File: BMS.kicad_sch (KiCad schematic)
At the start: 36 parts, among them J2 BMS1OTP, J3 BMS2OTP, U1 EL3H7, U3 ISO1640BDR, U4 BQ7695201PFBR, U6 ISO1640BDR

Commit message: time flies when you're kicadding :(
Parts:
- C18, C19, C2, C20, C26: footprint Capacitor_SMD:C_0805_2012Metric_Pad1.18x1.45mm_HandSolder -> Capacitor_SMD:C_0805_2012Metric
- R13: footprint Resistor_SMD:R_0805_2012Metric -> Resistor_SMD:R_0805_2012Metric_Pad1.20x1.40mm_HandSolder
- R18, R19, R20: footprint Resistor_SMD:R_0805_2012Metric_Pad1.20x1.40mm_HandSolder -> Resistor_SMD:R_0805_2012Metric
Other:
- note added: "I2C Pullup resistors need to be on the OTP circuit"
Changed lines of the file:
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@@
     (effects (font (size 2.5 2.5) (thickness 0.5) bold) (justify left bottom))
+  )
+  (text "I2C Pullup resistors need to be \non the OTP circuit"
+    (at 104.14 87.63 0)
+    (effects (font (size 1.27 1.27)) (justify left bottom))
   )
   (label "cell16" (at 200.66 210.185 0) (fields_autoplaced)
@@
       (effects (font (size 1.27 1.27)) (justify right))
     )
-    (property "Footprint" "Capacitor_SMD:C_0805_2012Metric_Pad1.18x1.45mm_HandSolder" (at 284.1498 89.535 0)
+    (property "Footprint" "Capacitor_SMD:C_0805_2012Metric" (at 284.1498 89.535 0)
       (effects (font (size 1.27 1.27)) hide)
     )
@@
       (effects (font (size 1.27 1.27)) (justify right))
     )
-    (property "Footprint" "Capacitor_SMD:C_0805_2012Metric_Pad1.18x1.45mm_HandSolder" (at 372.4148 28.575 0)
+    (property "Footprint" "Capacitor_SMD:C_0805_2012Metric" (at 372.4148 28.575 0)
       (effects (font (size 1.27 1.27)) hide)
     )
@@
       (effects (font (size 1.27 1.27)) (justify right))
     )
-    (property "Footprint" "Capacitor_SMD:C_0805_2012Metric_Pad1.18x1.45mm_HandSolder" (at 111.4298 33.655 0)
+    (property "Footprint" "Capacitor_SMD:C_0805_2012Metric" (at 111.4298 33.655 0)
       (effects (font (size 1.27 1.27)) hide)
     )
@@
       (effects (font (size 1.27 1.27)))
     )
-    (property "Footprint" "Resistor_SMD:R_0805_2012Metric_Pad1.20x1.40mm_HandSolder" (at 384.429 27.559 90)
+    (property "Footprint" "Resistor_SMD:R_0805_2012Metric" (at 384.429 27.559 90)
       (effects (font (size 1.27 1.27)) hide)
     )
@@
       (effects (font (size 1.27 1.27)) (justify right))
     )
-    (property "Footprint" "Capacitor_SMD:C_0805_2012Metric_Pad1.18x1.45mm_HandSolder" (at 30.7848 94.615 0)
+    (property "Footprint" "Capacitor_SMD:C_0805_2012Metric" (at 30.7848 94.615 0)
       (effects (font (size 1.27 1.27)) hide)
     )
@@
       (effects (font (size 1.27 1.27)))
     )
-    (property "Footprint" "Resistor_SMD:R_0805_2012Metric_Pad1.20x1.40mm_HandSolder" (at 342.011 44.831 90)
+    (property "Footprint" "Resistor_SMD:R_0805_2012Metric" (at 342.011 44.831 90)
       (effects (font (size 1.27 1.27)) hide)
     )
@@
       (effects (font (size 1.27 1.27)) (justify right))
     )
-    (property "Footprint" "Capacitor_SMD:C_0805_2012Metric_Pad1.18x1.45mm_HandSolder" (at 29.5148 133.35 0)
+    (property "Footprint" "Capacitor_SMD:C_0805_2012Metric" (at 29.5148 133.35 0)
       (effects (font (size 1.27 1.27)) hide)
     )
@@
       (effects (font (size 1.27 1.27)) (justify right))
     )
-    (property "Footprint" "Capacitor_SMD:C_0805_2012Metric_Pad1.18x1.45mm_HandSolder" (at 355.6 30.1498 0)
+    (property "Footprint" "Capacitor_SMD:C_0805_2012Metric" (at 355.6 30.1498 0)
       (effects (font (size 1.27 1.27)) hide)
     )
@@
       (effects (font (size 1.27 1.27)) (justify right))
     )
-    (property "Footprint" "Capacitor_SMD:C_0805_2012Metric_Pad1.18x1.45mm_HandSolder" (at 119.0752 140.97 0)
+    (property "Footprint" "Capacitor_SMD:C_0805_2012Metric" (at 119.0752 140.97 0)
       (effects (font (size 1.27 1.27)) hide)
     )
@@
       (effects (font (size 1.27 1.27)))
     )
-    (property "Footprint" "Resistor_SMD:R_0805_2012Metric_Pad1.20x1.40mm_HandSolder" (at 131.064 32.639 90)
+    (property "Footprint" "Resistor_SMD:R_0805_2012Metric" (at 131.064 32.639 90)
       (effects (font (size 1.27 1.27)) hide)
     )
@@
       (effects (font (size 1.27 1.27)) (justify right))
     )
-    (property "Footprint" "Capacitor_SMD:C_0805_2012Metric_Pad1.18x1.45mm_HandSolder" (at 389.5852 114.935 0)
+    (property "Footprint" "Capacitor_SMD:C_0805_2012Metric" (at 389.5852 114.935 0)
       (effects (font (size 1.27 1.27)) hide)
     )
@@
       (effects (font (size 1.27 1.27)))
     )
-    (property "Footprint" "Resistor_SMD:R_0805_2012Metric_Pad1.20x1.40mm_HandSolder" (at 88.646 49.911 90)
+    (property "Footprint" "Resistor_SMD:R_0805_2012Metric" (at 88.646 49.911 90)
       (effects (font (size 1.27 1.27)) hide)
     )
@@
       (effects (font (size 1.27 1.27)) (justify right))
     )
-    (property "Footprint" "Capacitor_SMD:C_0805_2012Metric_Pad1.18x1.45mm_HandSolder" (at 119.0498 33.655 0)
+    (property "Footprint" "Capacitor_SMD:C_0805_2012Metric" (at 119.0498 33.655 0)
       (effects (font (size 1.27 1.27)) hide)
     )
@@
       (effects (font (size 1.27 1.27)))
     )
-    (property "Footprint" "Resistor_SMD:R_0805_2012Metric_Pad1.20x1.40mm_HandSolder" (at 342.011 42.291 90)
+    (property "Footprint" "Resistor_SMD:R_0805_2012Metric" (at 342.011 42.291 90)
       (effects (font (size 1.27 1.27)) hide)
     )
@@
       (effects (font (size 1.27 1.27)) (justify right))
     )
-    (property "Footprint" "Resistor_SMD:R_0805_2012Metric" (at 358.14 151.765 0)
+    (property "Footprint" "Resistor_SMD:R_0805_2012Metric_Pad1.20x1.40mm_HandSolder" (at 358.14 151.765 0)
       (effects (font (size 1.27 1.27)) hide)
     )
@@
       (effects (font (size 1.27 1.27)) (justify right))
     )
-    (property "Footprint" "Capacitor_SMD:C_0805_2012Metric_Pad1.18x1.45mm_HandSolder" (at 364.7948 28.575 0)
+    (property "Footprint" "Capacitor_SMD:C_0805_2012Metric" (at 364.7948 28.575 0)
       (effects (font (size 1.27 1.27)) hide)
     )
@@
       (effects (font (size 1.27 1.27)) (justify right))
     )
-    (property "Footprint" "Capacitor_SMD:C_0805_2012Metric_Pad1.18x1.45mm_HandSolder" (at 102.235 35.2298 0)
+    (property "Footprint" "Capacitor_SMD:C_0805_2012Metric" (at 102.235 35.2298 0)
       (effects (font (size 1.27 1.27)) hide)
     )
@@
       (effects (font (size 1.27 1.27)))
     )
-    (property "Footprint" "Resistor_SMD:R_0805_2012Metric_Pad1.20x1.40mm_HandSolder" (at 88.646 47.371 90)
+    (property "Footprint" "Resistor_SMD:R_0805_2012Metric" (at 88.646 47.371 90)
       (effects (font (size 1.27 1.27)) hide)
     )
@@
       (effects (font (size 1.27 1.27)) (justify right))
     )
-    (property "Footprint" "Capacitor_SMD:C_0805_2012Metric_Pad1.18x1.45mm_HandSolder" (at 301.9298 107.95 0)
-      (effects (font (size 1.27 1.27)) hide)
-    )
+    (property "Footprint" "Capacitor_SMD:C_0805_2012Metric" (at 301.9298 107.95 0)
+      (effects (font (size 1.27 1.27)) hide)
+    )

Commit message: new ADC layout
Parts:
- renumbered C2 to C10, C26 to C11, C20 to C12, C19 to C13, C2 to C14, C2 to C3, C18 to C4, C26 to C5, C20 to C6, C2 to C7, C19 to C8, C18 to C9, R18 to R11, R19 to R12, R20 to R16, R18 to R5, R19 to R6, R20 to R9, U4 to U2, U4 to U5

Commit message: literal piss and shit
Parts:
- C10, C13, C14, C3, C7, C8: value 1u -> 1uF
- C11, C5: value .47u -> 0.47uF
- C12, C6: value 100p -> 100pF
- C4, C9: value 4.7u -> 4.7uF
- R13: footprint Resistor_SMD:R_0805_2012Metric_Pad1.20x1.40mm_HandSolder -> Resistor_SMD:R_0805_2012Metric
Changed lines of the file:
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@@
       (effects (font (size 1.27 1.27)) (justify right))
     )
-    (property "Value" "4.7u" (at 288.925 94.615 0)
+    (property "Value" "4.7uF" (at 288.925 94.615 0)
       (effects (font (size 1.27 1.27)) (justify right))
     )
@@
       (effects (font (size 1.27 1.27)) (justify right))
     )
-    (property "Value" "1u" (at 377.19 33.655 0)
+    (property "Value" "1uF" (at 377.19 33.655 0)
       (effects (font (size 1.27 1.27)) (justify right))
     )
@@
       (effects (font (size 1.27 1.27)) (justify right))
     )
-    (property "Value" "100p" (at 104.775 38.735 0)
+    (property "Value" "100pF" (at 104.775 38.735 0)
       (effects (font (size 1.27 1.27)) (justify right))
     )
@@
       (effects (font (size 1.27 1.27)) (justify right))
     )
-    (property "Value" "4.7u" (at 35.56 99.695 0)
+    (property "Value" "4.7uF" (at 35.56 99.695 0)
       (effects (font (size 1.27 1.27)) (justify right))
     )
@@
       (effects (font (size 1.27 1.27)) (justify right))
     )
-    (property "Value" "1u" (at 25.4 138.43 0)
+    (property "Value" "1uF" (at 25.4 138.43 0)
       (effects (font (size 1.27 1.27)) (justify right))
     )
@@
       (effects (font (size 1.27 1.27)) (justify right))
     )
-    (property "Value" ".47u" (at 349.25 34.925 90)
+    (property "Value" "0.47uF" (at 349.25 34.925 90)
       (effects (font (size 1.27 1.27)) (justify right))
     )
@@
       (effects (font (size 1.27 1.27)) (justify right))
     )
-    (property "Value" "1u" (at 125.095 135.89 0)
+    (property "Value" "1uF" (at 125.095 135.89 0)
       (effects (font (size 1.27 1.27)) (justify right))
     )
@@
       (effects (font (size 1.27 1.27)) (justify right))
     )
-    (property "Value" "1u" (at 394.97 109.855 0)
+    (property "Value" "1uF" (at 394.97 109.855 0)
       (effects (font (size 1.27 1.27)) (justify right))
     )
@@
       (effects (font (size 1.27 1.27)) (justify right))
     )
-    (property "Value" "1u" (at 123.825 38.735 0)
+    (property "Value" "1uF" (at 123.825 38.735 0)
       (effects (font (size 1.27 1.27)) (justify right))
     )
@@
       (effects (font (size 1.27 1.27)) (justify right))
     )
-    (property "Footprint" "Resistor_SMD:R_0805_2012Metric_Pad1.20x1.40mm_HandSolder" (at 358.14 151.765 0)
+    (property "Footprint" "Resistor_SMD:R_0805_2012Metric" (at 358.14 151.765 0)
       (effects (font (size 1.27 1.27)) hide)
     )
@@
       (effects (font (size 1.27 1.27)) (justify right))
     )
-    (property "Value" "100p" (at 358.14 33.655 0)
+    (property "Value" "100pF" (at 358.14 33.655 0)
       (effects (font (size 1.27 1.27)) (justify right))
     )
@@
       (effects (font (size 1.27 1.27)) (justify right))
     )
-    (property "Value" ".47u" (at 95.885 40.005 90)
+    (property "Value" "0.47uF" (at 95.885 40.005 90)
       (effects (font (size 1.27 1.27)) (justify right))
     )
@@
       (effects (font (size 1.27 1.27)) (justify right))
     )
-    (property "Value" "1u" (at 296.545 113.03 0)
-      (effects (font (size 1.27 1.27)) (justify right))
-    )
+    (property "Value" "1uF" (at 296.545 113.03 0)
+      (effects (font (size 1.27 1.27)) (justify right))
+    )

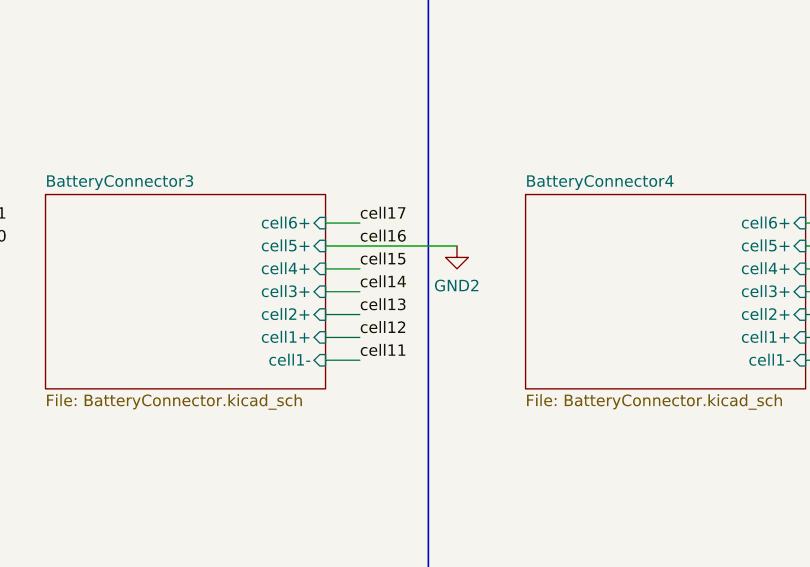
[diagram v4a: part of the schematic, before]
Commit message: fix gnd2
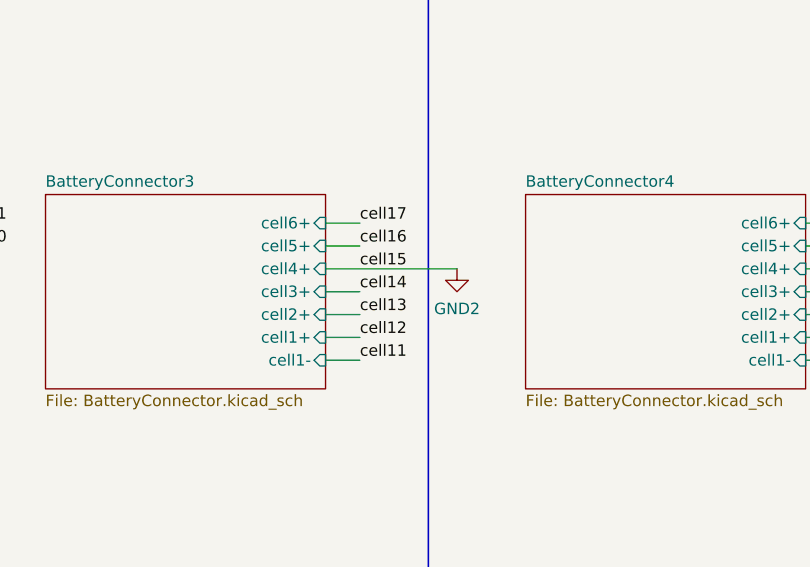
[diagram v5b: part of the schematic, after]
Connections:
- net cell15 is gone; now on net GND2: U2.1 (VC15)
- net GND2: no longer U2.48 (VC16), U5.16 (VC0)
- new net cell16: U2.48 (VC16), U5.16 (VC0)
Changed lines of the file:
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@@
-    (stroke (width 0) (type default))
-  )
-  (wire (pts (xy 196.85 210.185) (xy 211.455 210.185))
     (stroke (width 0) (type default))
   )
@@
     (stroke (width 0) (type default))
   )
+  (wire (pts (xy 196.85 210.185) (xy 200.66 210.185))
+    (stroke (width 0) (type default))
+  )
   (wire (pts (xy 294.64 212.725) (xy 298.45 212.725))
     (stroke (width 0) (type default))
@@
     (stroke (width 0) (type default))
   )
-  (wire (pts (xy 196.85 212.725) (xy 200.66 212.725))
+  (wire (pts (xy 196.85 212.725) (xy 211.455 212.725))
     (stroke (width 0) (type default))
   )
@@
     )
   )
-  (symbol (lib_id "power:GND2") (at 211.455 210.185 0) (unit 1)
+  (symbol (lib_id "power:GND2") (at 211.455 212.725 0) (unit 1)
     (in_bom yes) (on_board yes) (dnp no) (fields_autoplaced)
-    (property "Reference" "#PWR028" (at 211.455 216.535 0)
+    (property "Reference" "#PWR028" (at 211.455 219.075 0)
       (effects (font (size 1.27 1.27)) hide)
     )
-    (property "Value" "GND2" (at 211.455 214.63 0)
+    (property "Value" "GND2" (at 211.455 217.17 0)
       (effects (font (size 1.27 1.27)))
     )
-    (property "Footprint" "" (at 211.455 210.185 0)
+    (property "Footprint" "" (at 211.455 212.725 0)
       (effects (font (size 1.27 1.27)) hide)
     )
-    (property "Datasheet" "" (at 211.455 210.185 0)
+    (property "Datasheet" "" (at 211.455 212.725 0)
       (effects (font (size 1.27 1.27)) hide)
     )

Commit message: TI GNDing is weirddd
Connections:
- net PACK1+ is gone; now on net cell32: R11.1, R12.1
- net cell0 is gone; now on net GND1: U2.16 (VC0)
- net cell16 is gone; now on net GND2: U2.48 (VC16), U5.16 (VC0)
- net GND2: no longer U2.1 (VC15)
- new net cell15: U2.1 (VC15)
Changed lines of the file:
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@@
   (junction (at 112.395 33.655) (diameter 0) (color 0 0 0 0)
+  )
+  (junction (at 111.76 222.885) (diameter 0) (color 0 0 0 0)
   )
   (junction (at 282.575 66.675) (diameter 0) (color 0 0 0 0)
@@
     (stroke (width 0) (type default))
   )
+  (wire (pts (xy 111.76 220.345) (xy 111.76 222.885))
+    (stroke (width 0) (type default))
+  )
   (wire (pts (xy 356.87 28.575) (xy 356.87 31.115))
     (stroke (width 0) (type default))
@@
     (stroke (width 0) (type default))
   )
+  (wire (pts (xy 346.075 43.815) (xy 349.25 43.815))
+    (stroke (width 0) (type default))
+  )
   (wire (pts (xy 196.85 222.885) (xy 200.66 222.885))
     (stroke (width 0) (type default))
@@
     (stroke (width 0) (type default))
   )
-  (wire (pts (xy 196.85 210.185) (xy 200.66 210.185))
+  (wire (pts (xy 196.85 210.185) (xy 211.455 210.185))
     (stroke (width 0) (type default))
   )
@@
     (stroke (width 0) (type default))
   )
+  (wire (pts (xy 196.85 212.725) (xy 200.66 212.725))
+    (stroke (width 0) (type default))
+  )
   (wire (pts (xy 359.41 119.38) (xy 388.62 119.38))
     (stroke (width 0) (type default))
@@
     (stroke (width 0) (type default))
   )
+  (wire (pts (xy 349.25 41.275) (xy 349.25 43.815))
+    (stroke (width 0) (type default))
+  )
   (wire (pts (xy 196.85 217.805) (xy 200.66 217.805))
     (stroke (width 0) (type default))
@@
     (stroke (width 0) (type default))
   )
+  (wire (pts (xy 346.075 41.275) (xy 349.25 41.275))
+    (stroke (width 0) (type default))
+  )
   (wire (pts (xy 24.13 33.655) (xy 31.75 33.655))
     (stroke (width 0) (type default))
@@
   )
   (wire (pts (xy 339.09 217.805) (xy 342.9 217.805))
-    (stroke (width 0) (type default))
-  )
-  (wire (pts (xy 196.85 212.725) (xy 211.455 212.725))
     (stroke (width 0) (type default))
   )
@@
     (effects (font (size 1.27 1.27)) (justify left bottom))
   )
-  (label "cell0" (at 111.76 220.345 0) (fields_autoplaced)
-    (effects (font (size 1.27 1.27)) (justify left bottom))
-  )
   (label "cell12" (at 24.13 38.735 0) (fields_autoplaced)
     (effects (font (size 1.27 1.27)) (justify left bottom))
   )
   (label "cell19" (at 277.495 56.515 0) (fields_autoplaced)
+    (effects (font (size 1.27 1.27)) (justify left bottom))
+  )
+  (label "cell32" (at 349.25 41.275 0) (fields_autoplaced)
     (effects (font (size 1.27 1.27)) (justify left bottom))
   )
@@
     (effects (font (size 1.27 1.27)) (justify left bottom))
   )
-  (label "PACK1+" (at 346.075 43.815 0) (fields_autoplaced)
-    (effects (font (size 1.27 1.27)) (justify left bottom))
-  )
   (label "cell31" (at 277.495 26.035 0) (fields_autoplaced)
     (effects (font (size 1.27 1.27)) (justify left bottom))
@@
     (effects (font (size 1.27 1.27)) (justify left bottom))
   )
-  (label "cell0" (at 24.13 69.215 0) (fields_autoplaced)
+  (label "VC0" (at 24.13 69.215 0) (fields_autoplaced)
     (effects (font (size 1.27 1.27)) (justify left bottom))
   )
@@
     (effects (font (size 1.27 1.27)) (justify left bottom))
   )
-  (label "PACK1+" (at 346.075 41.275 0) (fields_autoplaced)
-    (effects (font (size 1.27 1.27)) (justify left bottom))
-  )
   (label "BMS1Reset" (at 85.09 69.215 0) (fields_autoplaced)
     (effects (font (size 1.27 1.27)) (justify left bottom))
@@
   )
   (label "cell20" (at 254 215.265 0) (fields_autoplaced)
+    (effects (font (size 1.27 1.27)) (justify left bottom))
+  )
+  (label "VC0" (at 111.76 220.345 0) (fields_autoplaced)
     (effects (font (size 1.27 1.27)) (justify left bottom))
   )
@@
     )
   )
-  (symbol (lib_id "power:GND2") (at 211.455 212.725 0) (unit 1)
+  (symbol (lib_id "power:GND2") (at 211.455 210.185 0) (unit 1)
     (in_bom yes) (on_board yes) (dnp no) (fields_autoplaced)
-    (property "Reference" "#PWR028" (at 211.455 219.075 0)
+    (property "Reference" "#PWR028" (at 211.455 216.535 0)
       (effects (font (size 1.27 1.27)) hide)
     )
-    (property "Value" "GND2" (at 211.455 217.17 0)
+    (property "Value" "GND2" (at 211.455 214.63 0)
       (effects (font (size 1.27 1.27)))
     )
-    (property "Footprint" "" (at 211.455 212.725 0)
+    (property "Footprint" "" (at 211.455 210.185 0)
       (effects (font (size 1.27 1.27)) hide)
     )
-    (property "Datasheet" "" (at 211.455 212.725 0)
+    (property "Datasheet" "" (at 211.455 210.185 0)
       (effects (font (size 1.27 1.27)) hide)
     )
